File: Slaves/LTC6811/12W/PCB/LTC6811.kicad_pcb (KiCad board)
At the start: 2 copper layers, 195 x 50 mm, 128 parts, among them J1 Cells, J2 PB MB, J3 PA MA, J4 Temp, Q1 NSV1C201MZ4, Q10 TSM2323, Q11 TSM2323, Q12 TSM2323, Q13 TSM2323, Q2 TSM2323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

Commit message: finish balancing
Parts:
- moved FB1 56.6 mm to (181.7, 101.0)
- moved R2 49.6 mm to (176.8, 101.0), turned to 180 degrees
- moved D13 21.8 mm to (154.8, 88.7), turned to -90 degrees
- moved D14 18.2 mm to (151.5, 88.7), turned to -90 degrees
- moved D15 15.2 mm to (148.2, 88.7), turned to -90 degrees
- moved C23 4.22 mm to (188.7, 61.5)
- moved D11 4.20 mm to (191.5, 60.4)
- moved C24 4.06 mm to (188.7, 57.5)
- moved C22 4.04 mm to (188.7, 65.4)
- moved D10 4.02 mm to (191.5, 64.4)
- moved D12 4.02 mm to (191.5, 56.5)
- moved C21 3.99 mm to (188.7, 69.4)
- moved D9 3.98 mm to (191.5, 68.3)
- moved C20 3.94 mm to (188.7, 73.3)
- moved D8 3.93 mm to (191.5, 72.3)
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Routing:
- net /cell1/S: track 0.00 -> 42.3 mm
- net /cell12/S: track 0.00 -> 32.2 mm
- net /cell11/S: track 0.00 -> 30.9 mm
- net /cell2/S: track 0.00 -> 30.6 mm
- net /cell1/C: track 0.00 -> 29.7 mm
- net /cell10/S: track 0.00 -> 29.6 mm
- net /cell3/S: track 0.00 -> 29.3 mm
- net /cell9/S: track 0.00 -> 28.3 mm
- net /cell4/S: track 0.00 -> 28.1 mm
- net /cell12/C: track 0.00 -> 28.0 mm
- net /cell11/C: track 0.00 -> 27.1 mm
- net /cell5/S: track 0.00 -> 26.9 mm
- net /cell8/S: track 0.00 -> 26.8 mm
- net /cell2/C: track 0.00 -> 26.0 mm
- net /cell6/S: track 0.00 -> 25.9 mm
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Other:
- board size 195 x 50 mm -> 195 x 48.5 mm

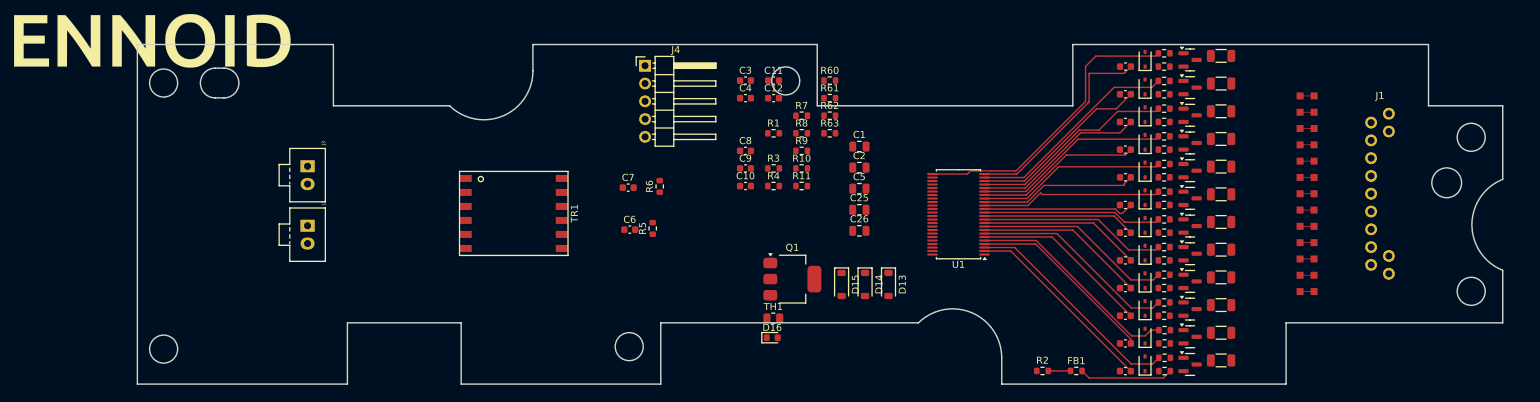
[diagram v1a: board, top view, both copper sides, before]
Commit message: Finish most routing
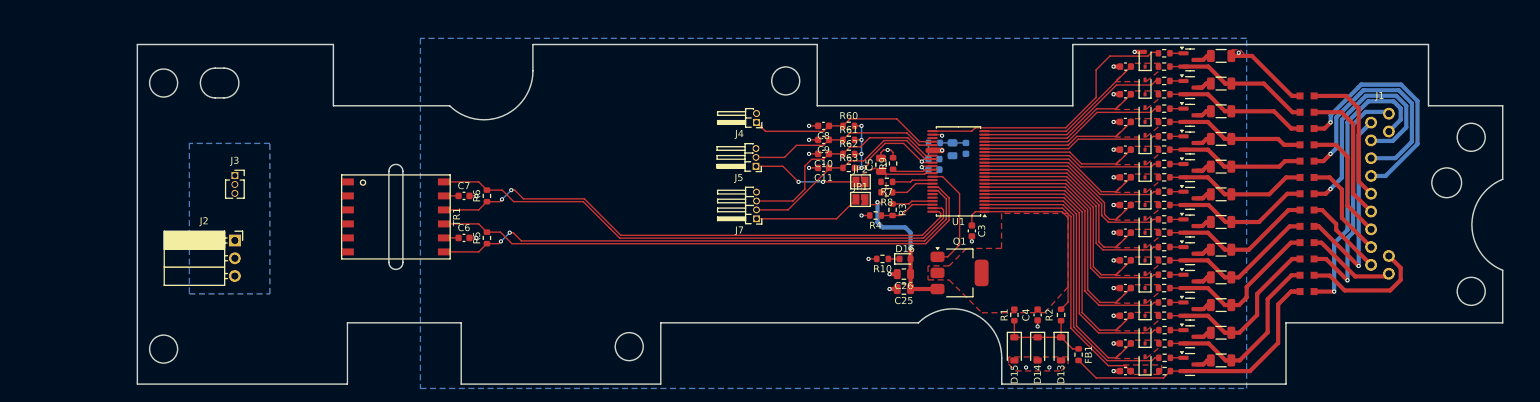
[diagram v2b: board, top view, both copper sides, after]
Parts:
- added J5: Conn_01x03, Connector_PinHeader_1.27mm:PinHeader_1x03_P1.27mm_Horizontal, F.Cu at (135.9, 71.8)
- added J7: Conn_01x04, Connector_PinHeader_1.27mm:PinHeader_1x04_P1.27mm_Horizontal, F.Cu at (136.0, 79.3)
- added JP1: SolderJumper_2_Open, Jumper:SolderJumper-2_P1.3mm_Open_Pad1.0x1.5mm, F.Cu at (150.8, 76.5)
- added JP2: SolderJumper_2_Open, Jumper:SolderJumper-2_P1.3mm_Open_Pad1.0x1.5mm, F.Cu at (150.8, 74.0)
- C1, C2: footprint Capacitor_SMD:C_0805_2012Metric -> Capacitor_SMD:C_0603_1608Metric; moved to B.Cu
- C12, LOGO1, R11, TH1: moved to B.Cu
- J2: value PB MB -> PA MA; footprint ENNOID:Pin_1x02-XL -> Connector_PinSocket_2.54mm:PinSocket_1x03_P2.54mm_Horizontal
- J3: value PA MA -> PA MB; footprint ENNOID:Pin_1x02-XL -> Connector_PinSocket_1.27mm:PinSocket_1x03_P1.27mm_Vertical
- J4: value Temp -> Conn_01x02; footprint Connector_PinHeader_2.54mm:PinHeader_1x05_P2.54mm_Horizontal -> Connector_PinHeader_1.27mm:PinHeader_1x02_P1.27mm_Horizontal
- moved LOGO1 150.0 mm to (197.8, 78.5), turned to 90 degrees
- moved C4 52.0 mm to (176.2, 93.0), turned to -90 degrees
- moved R1 43.1 mm to (172.8, 93.0), turned to 90 degrees
- moved C3 38.8 mm to (166.8, 81.0), turned to -90 degrees
- moved TH1 35.2 mm to (164.0, 69.3), turned to -90 degrees
- moved C12 28.4 mm to (165.9, 69.2), turned to -90 degrees
- moved D15 26.3 mm to (172.8, 97.8)
- moved D13 26.3 mm to (179.5, 97.8)
- moved D14 26.3 mm to (176.2, 97.8)
- moved R6 24.7 mm to (97.5, 76.0)
- moved Q1 23.9 mm to (165.0, 87.0)
- moved R5 23.7 mm to (97.5, 82.0)
- moved C6 23.7 mm to (94.2, 82.0)
- moved C7 23.5 mm to (94.2, 76.0)
- moved D16 22.1 mm to (157.2, 85.0)
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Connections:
- C10 pad 1: /T4 -> /T4/SDA
- C11 pad 1: /T5 -> /T5/SCL
- C9 pad 1: /T3 -> /T3/GPIO
- J4 pad 1: GND -> /T2
- J4 pad 2: /T2 -> GND
- R5 pad 1: /IPB -> /IPA
- R5 pad 2: /IMB -> /IMA
- R6 pad 1: /IPA -> /IPB
- R6 pad 2: /IMA -> /IMB
- R61 pad 1: /T3 -> /T3/GPIO
- R62 pad 1: /T4 -> /T4/SDA
- R63 pad 1: /T5 -> /T5/SCL
- TR1 pad 1: Net-(J3-Pin_1) -> Net-(J3-Pin_2)
- TR1 pad 10: /IPA -> /IPB
- TR1 pad 12: /IMA -> /IMB
- TR1 pad 3: Net-(J3-Pin_2) -> Net-(J3-Pin_1)
- TR1 pad 4: Net-(J2-Pin_1) -> Net-(J2-Pin_2)
- TR1 pad 6: Net-(J2-Pin_2) -> Net-(J2-Pin_1)
- TR1 pad 7: /IPB -> /IPA
- TR1 pad 9: /IMB -> /IMA
- U1 pad 29: /T3 -> /T3/GPIO
- U1 pad 32: /T4 -> /T4/SDA
- U1 pad 33: /T5 -> /T5/SCL
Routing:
- net /IMA: track 0.00 -> 80.9 mm
- net /IPA: track 0.00 -> 80.0 mm, vias 0 -> 2
- net /IMB: track 0.00 -> 79.0 mm
- net /IPB: track 0.00 -> 77.6 mm, vias 0 -> 2
- net GND: track 0.00 -> 44.9 mm, vias 0 -> 31
- net Net-(J1-Pin_13): track 0.00 -> 41.1 mm, vias 0 -> 1
- net Net-(J1-Pin_11): track 0.00 -> 34.3 mm, vias 0 -> 1
- net Net-(J1-Pin_5): track 0.00 -> 33.6 mm, vias 0 -> 1
- net Net-(J1-Pin_3): track 0.00 -> 33.4 mm, vias 0 -> 1
- net Net-(J1-Pin_7): track 0.00 -> 33.1 mm, vias 0 -> 1
- net /T4/SDA: track 0.00 -> 31.9 mm
- net /T5/SCL: track 0.00 -> 30.4 mm
- net Net-(J1-Pin_9): track 0.00 -> 29.7 mm, vias 0 -> 1
- net Net-(U1-V+): track 0.00 -> 29.0 mm
- net /Vreg: track 0.00 -> 28.0 mm, vias 0 -> 2
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- added copper zone on F.Cu, net /Vreg
- added copper zone on F.Cu, net /cell1/C
- added copper zone on F.Cu, net /cell10/C
- added copper zone on F.Cu, net /cell10/CM
- added copper zone on F.Cu, net /cell11/C
- added copper zone on F.Cu, net /cell12/C
- added copper zone on F.Cu, net /cell2/C
- added copper zone on F.Cu, net /cell3/C
- added copper zone on F.Cu, net /cell4/C
- added copper zone on F.Cu, net /cell5/C
- added copper zone on F.Cu, net /cell6/C
- added copper zone on F.Cu, net /cell7/C
- added copper zone on F.Cu, net /cell8/C
- added copper zone on B.Cu, net GND
- added copper zone on F.Cu, net GND
- added copper zone on B.Cu, net GNDCHA
- added copper zone on F.Cu, net Net-(C4-Pad1)
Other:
- outline, holes or cut-outs redrawn

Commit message: Finish Rev1
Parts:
- J3: footprint Connector_PinSocket_1.27mm:PinSocket_1x03_P1.27mm_Vertical -> Connector_PinSocket_2.54mm:PinSocket_1x03_P2.54mm_Horizontal
- moved J4 6.07 mm to (134.0, 59.8)
- moved J5 6.07 mm to (133.9, 66.0)
- moved J7 6.07 mm to (134.0, 73.5)
- moved JP1 2.50 mm to (150.8, 74.0)
- moved JP2 2.50 mm to (150.8, 76.5)
- moved C3 0.28 mm to (166.8, 81.3)
- moved R9 0.23 mm to (155.7, 71.4)
- moved C5 0.22 mm to (154.0, 71.6)
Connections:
- TR1 pad 1: Net-(J3-Pin_2) -> Net-(J3-Pin_1)
- TR1 pad 3: Net-(J3-Pin_1) -> Net-(J3-Pin_2)
- TR1 pad 4: Net-(J2-Pin_2) -> Net-(J2-Pin_1)
- TR1 pad 6: Net-(J2-Pin_1) -> Net-(J2-Pin_2)
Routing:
- net Net-(J3-Pin_2): track 0.00 -> 17.1 mm
- net Net-(J2-Pin_1): track 0.00 -> 17.1 mm
- net Net-(J3-Pin_1): track 0.00 -> 16.5 mm
- net Net-(J2-Pin_2): track 0.00 -> 16.5 mm
- net Net-(J5-Pin_1): track 15.2 -> 27.6 mm, vias 2 -> 0
- net /T2: track 27.7 -> 31.3 mm
- net /T1: track 3.70 -> 5.85 mm, vias 0 -> 1
- net /T3/GPIO: track 27.4 -> 29.5 mm
- net /T4/SDA: track 31.9 -> 30.3 mm
- net Net-(J7-Pin_1): track 15.3 -> 16.4 mm

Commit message: more updates
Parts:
- removed J7: Conn_01x04, Connector_PinHeader_1.27mm:PinHeader_1x04_P1.27mm_Horizontal
- removed JP1, JP2: SolderJumper_2_Open, Jumper:SolderJumper-2_P1.3mm_Open_Pad1.0x1.5mm
- added R90: 0, Resistor_SMD:R_1206_3216Metric, F.Cu at (157.9, 81.8)
- C1, C12, C2, R11: moved to F.Cu
- C25, C26, C5: footprint Capacitor_SMD:C_0805_2012Metric -> Capacitor_SMD:C_0603_1608Metric
- J2: value PA MA -> Conn_01x02; footprint Connector_PinSocket_2.54mm:PinSocket_1x03_P2.54mm_Horizontal -> Connector_JST:JST_XA_S02B-XASK-1_1x02_P2.50mm_Horizontal
- J3: value PA MB -> Conn_01x02; footprint Connector_PinSocket_2.54mm:PinSocket_1x03_P2.54mm_Horizontal -> Connector_JST:JST_XA_S02B-XASK-1_1x02_P2.50mm_Horizontal
- J4: footprint Connector_PinHeader_1.27mm:PinHeader_1x02_P1.27mm_Horizontal -> Connector_JST:JST_XA_S02B-XASK-1_1x02_P2.50mm_Horizontal
- J5: value Conn_01x03 -> Conn_01x06; footprint Connector_PinHeader_1.27mm:PinHeader_1x03_P1.27mm_Horizontal -> Connector_PinHeader_2.00mm:PinHeader_1x06_P2.00mm_Vertical
- TH1: footprint Resistor_SMD:R_0805_2012Metric -> Resistor_SMD:R_0603_1608Metric; moved to F.Cu
- moved R6 30.3 mm to (125.1, 88.5)
- moved C6 28.4 mm to (121.8, 88.5)
- moved C7 28.4 mm to (121.8, 82.5)
- moved TR1 28.4 mm to (112.1, 85.5)
- moved R5 27.6 mm to (125.1, 82.5)
- moved J2 25.4 mm to (86.9, 83.8), turned to -90 degrees
- moved J3 25.4 mm to (86.9, 73.8), turned to -90 degrees
- moved R11 20.4 mm to (178.2, 80.0)
- moved TH1 18.7 mm to (178.2, 81.5), turned to 180 degrees
- moved C12 18.5 mm to (178.2, 83.0), turned to 180 degrees
- moved R3 16.8 mm to (172.0, 80.8), turned to 90 degrees
- moved R4 16.7 mm to (169.5, 81.7)
- moved C3 15.7 mm to (177.3, 93.0)
- moved J4 14.8 mm to (125.8, 72.0)
- moved C11 13.2 mm to (158.5, 74.5), turned to -90 degrees
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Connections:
- C25 pad 1: /Vreg -> Net-(D16-A)
- C26 pad 1: /Vreg -> Net-(D16-A)
- D16 pad 2: /Vreg -> Net-(D16-A)
- J5 pad 1: Net-(J5-Pin_1) -> /Vreg
- J5 pad 2: /T3/GPIO -> /Vref2
- J5 pad 3: GND -> /T5/SCL
- Q1 pad 3: /Vreg -> Net-(D16-A)
- R5 pad 1: /IPA -> /IMB
- R5 pad 2: /IMA -> /IPB
- R6 pad 1: /IPB -> /IMA
- R6 pad 2: /IMB -> /IPA
- TR1 pad 10: /IPB -> /IMB
- TR1 pad 12: /IMB -> /IPB
- TR1 pad 7: /IPA -> /IMA
- TR1 pad 9: /IMA -> /IPA
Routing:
- net /Vref2: track 26.2 -> 73.0 mm, vias 5 -> 3
- net Net-(J5-Pin_1): track 27.6 -> 0.00 mm
- net /IPB: track 77.6 -> 54.2 mm, vias 2 -> 0
- net /IMB: track 79.0 -> 57.4 mm
- net /T2: track 31.3 -> 48.8 mm
- net Net-(J7-Pin_1): track 16.4 -> 0.00 mm
- net /IPA: track 80.0 -> 66.0 mm, vias 2 -> 0
- net /T1: track 5.85 -> 19.6 mm, vias 1 -> 0
- net /IMA: track 80.9 -> 67.9 mm
- net Net-(U1-V+): track 29.0 -> 18.1 mm
- net /Vreg: track 27.7 -> 38.6 mm, vias 2 -> 0
- net /cell9/S: track 35.5 -> 25.4 mm
- net /cell5/S: track 25.7 -> 15.5 mm
- net /cell2/S: track 28.0 -> 17.9 mm
- net /cell11/S: track 41.5 -> 31.3 mm
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- removed copper zone on B.Cu, net GNDCHA
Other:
- outline, holes or cut-outs redrawn
- board text added: "C12+1"
- board text added: "D5+1"
- board text added: "Q2+1"
- board text added: "R14+3"
- board text added: "R15+3"
- board text added: "R16+3"
